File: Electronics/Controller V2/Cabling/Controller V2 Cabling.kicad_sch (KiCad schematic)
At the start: 12 parts, among them J1 Conn_01x30, J10 Spare Valve, J11 Battery, J2 GPIO, J3 Tractor CAN, J4 Scraper CAN, J5 Spare CAN, J6 Front Height, J7 Rear Height, J8 Front Apron/Dump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

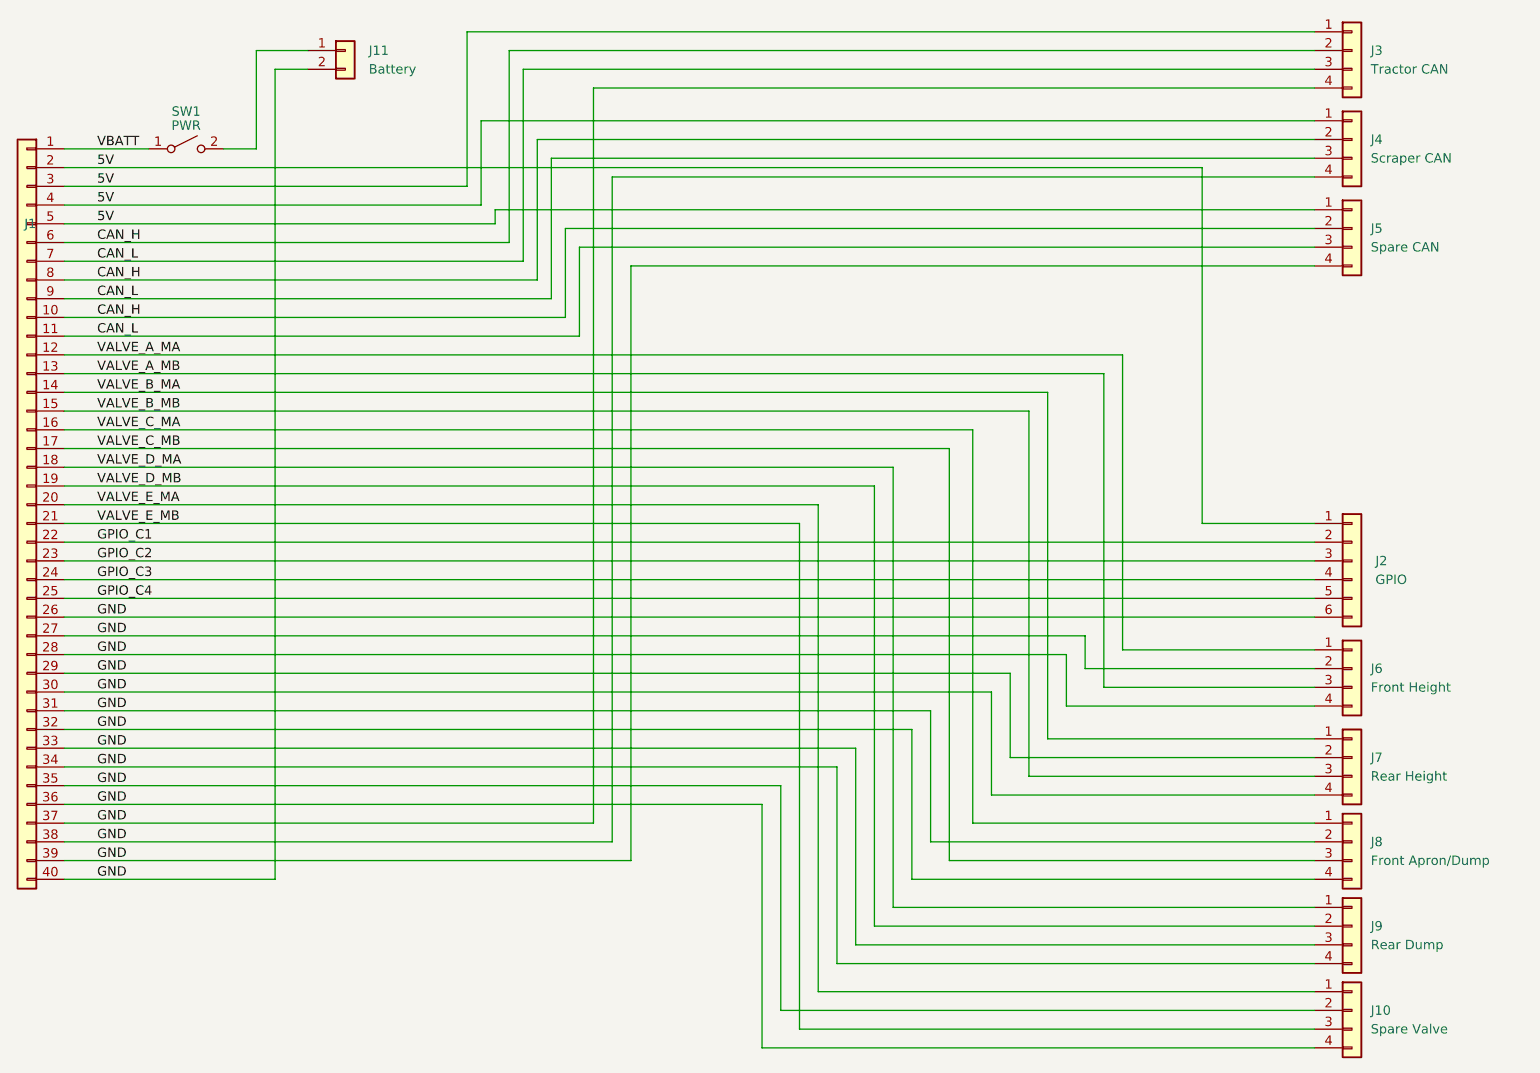
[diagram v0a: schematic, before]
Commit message: Reordered main connector.
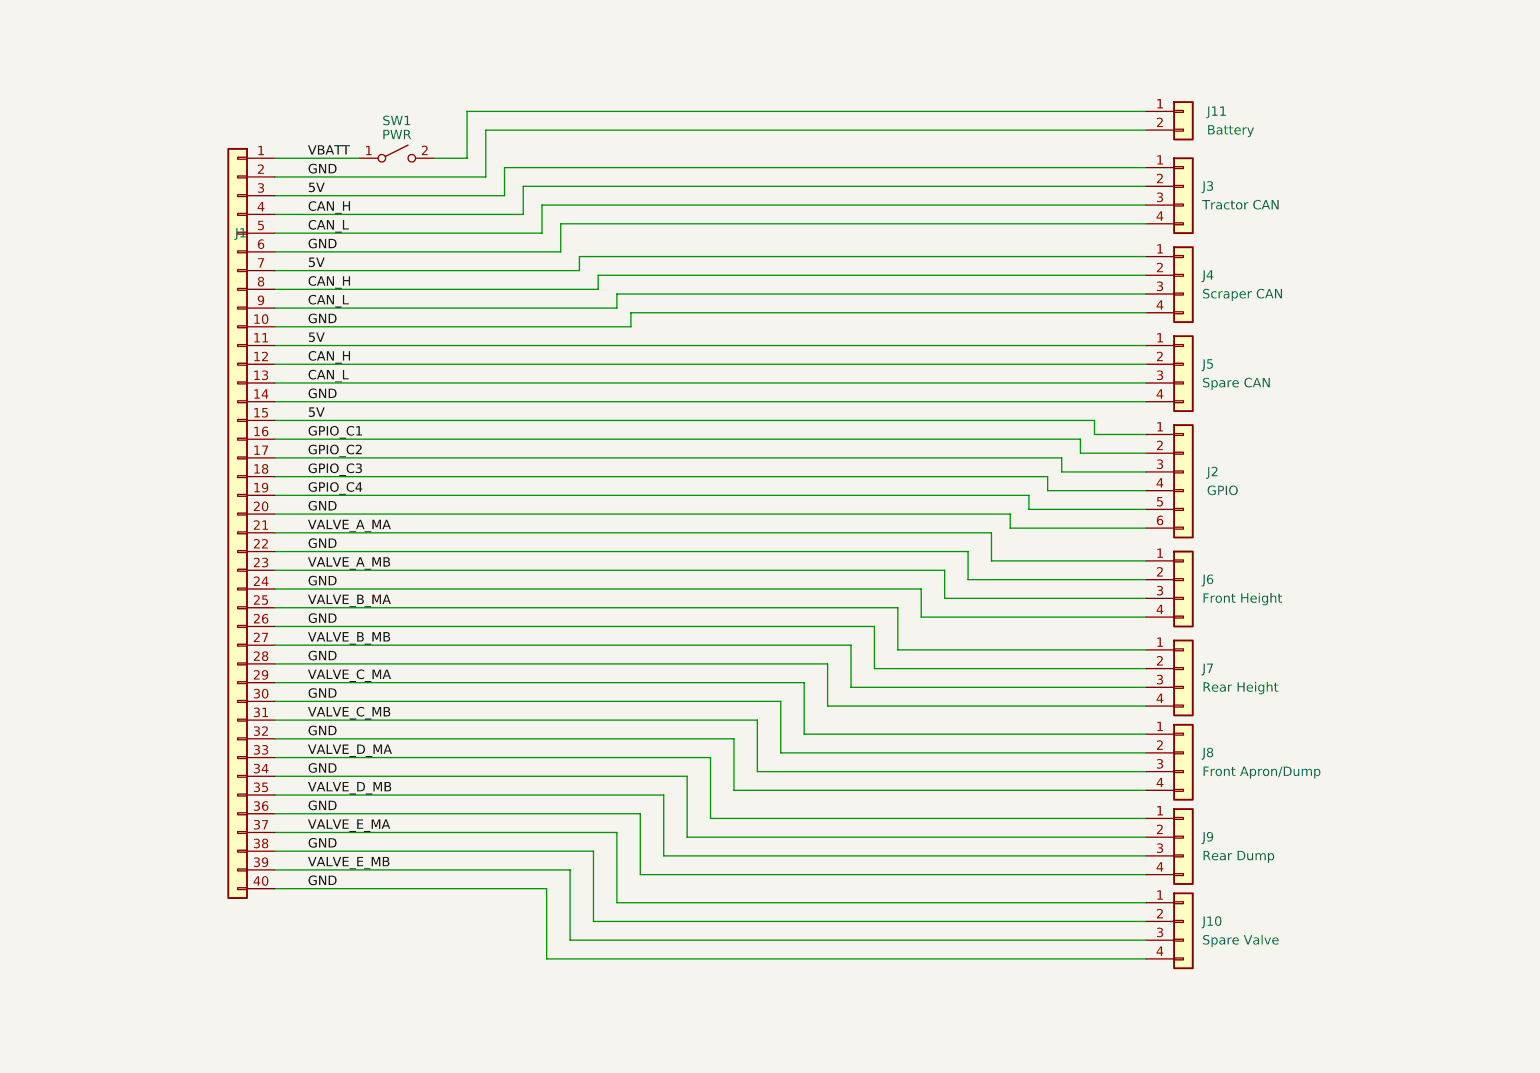
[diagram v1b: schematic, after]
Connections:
- net 5V: now also J1.11 (Pin_11), J1.15 (Pin_15), J1.7 (Pin_7); no longer J1.2 (Pin_2), J1.4 (Pin_4), J1.5 (Pin_5)
- net CAN_H: now also J1.12 (Pin_12), J1.4 (Pin_4); no longer J1.10 (Pin_10), J1.6 (Pin_6)
- net CAN_L: now also J1.13 (Pin_13), J1.5 (Pin_5); no longer J1.11 (Pin_11), J1.7 (Pin_7)
- net GND: now also J1.10 (Pin_10), J1.14 (Pin_14), J1.2 (Pin_2), J1.20 (Pin_20), J1.22 (Pin_22), J1.24 (Pin_24), J1.6 (Pin_6), J9.2 (Pin_2); no longer J1.27 (Pin_27), J1.29 (Pin_29), J1.31 (Pin_31), J1.33 (Pin_33), J1.35 (Pin_35), J1.37 (Pin_37), J1.39 (Pin_39), J9.3 (Pin_3)
- net GPIO_C1: now also J1.16 (Pin_16); no longer J1.22 (Pin_22)
- net GPIO_C2: now also J1.17 (Pin_17); no longer J1.23 (Pin_23)
- net GPIO_C3: now also J1.18 (Pin_18); no longer J1.24 (Pin_24)
- net GPIO_C4: now also J1.19 (Pin_19); no longer J1.25 (Pin_25)
- net VALVE_A_MA: now also J1.21 (Pin_21); no longer J1.12 (Pin_12)
- net VALVE_A_MB: now also J1.23 (Pin_23); no longer J1.13 (Pin_13)
- net VALVE_B_MA: now also J1.25 (Pin_25); no longer J1.14 (Pin_14)
- net VALVE_B_MB: now also J1.27 (Pin_27); no longer J1.15 (Pin_15)
- net VALVE_C_MA: now also J1.29 (Pin_29); no longer J1.16 (Pin_16)
- net VALVE_C_MB: now also J1.31 (Pin_31); no longer J1.17 (Pin_17)
- net VALVE_D_MA: now also J1.33 (Pin_33); no longer J1.18 (Pin_18)
- net VALVE_D_MB: now also J1.35 (Pin_35), J9.3 (Pin_3); no longer J1.19 (Pin_19), J9.2 (Pin_2)
- net VALVE_E_MA: now also J1.37 (Pin_37); no longer J1.20 (Pin_20)
- net VALVE_E_MB: now also J1.39 (Pin_39); no longer J1.21 (Pin_21)
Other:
- moved on the sheet: J1, J10, J11, J2, J3, J4, J5, J6, J7, J8, J9, SW1

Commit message: Added AMP connectors. Working on PCB layout.
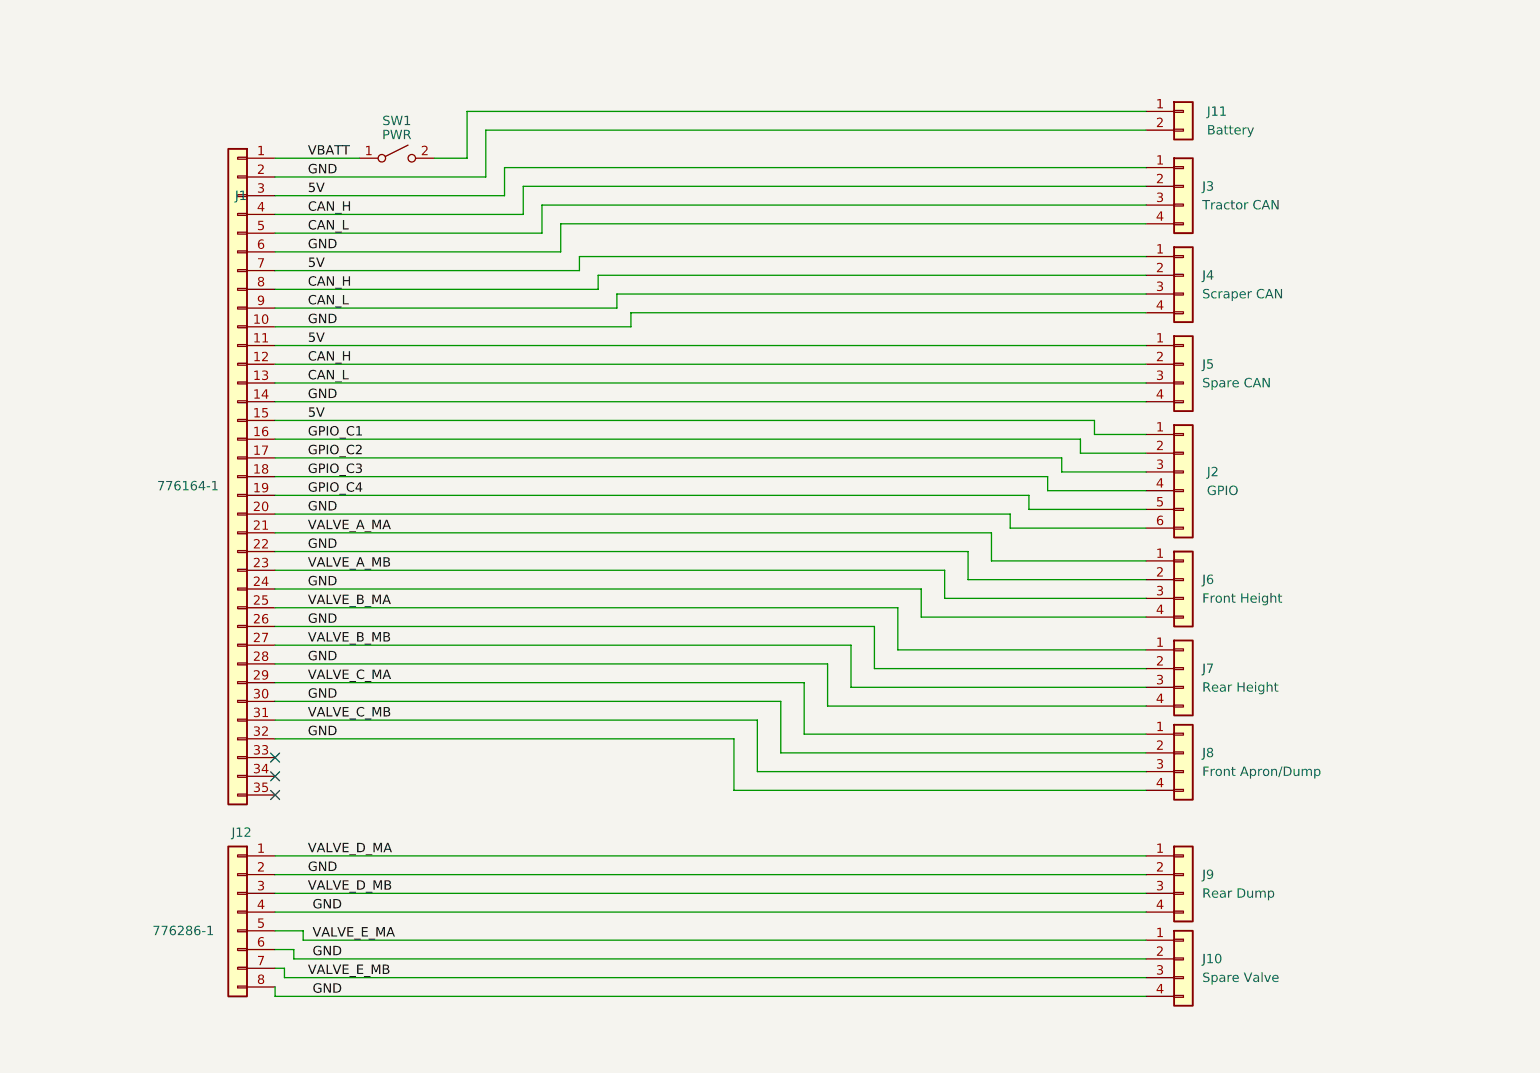
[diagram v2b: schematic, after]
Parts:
- added J12: 776286-1, symbol Connector_Generic:Conn_01x08
- J1: value Conn_01x30 -> 776164-1; symbol Connector_Generic:Conn_01x40 -> Connector_Generic:Conn_01x35
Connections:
- net GND: now also J12.2 (Pin_2), J12.4 (Pin_4), J12.6 (Pin_6), J12.8 (Pin_8); no longer J1.34 (Pin_34), J1.36 (Pin_36), J1.38 (Pin_38), J1.40 (Pin_40)
- net VALVE_D_MA: now also J12.1 (Pin_1); no longer J1.33 (Pin_33)
- net VALVE_D_MB: now also J12.3 (Pin_3); no longer J1.35 (Pin_35)
- net VALVE_E_MA: now also J12.5 (Pin_5); no longer J1.37 (Pin_37)
- net VALVE_E_MB: now also J12.7 (Pin_7); no longer J1.39 (Pin_39)
- no-connect marks 0 -> 3
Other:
- moved on the sheet: J10, J9

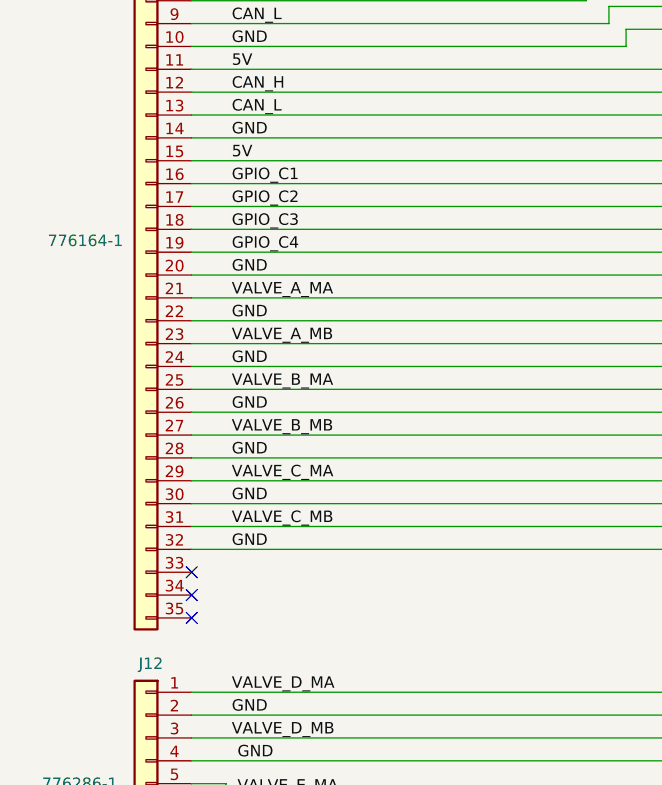
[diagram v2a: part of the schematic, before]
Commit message: Added missing ground connection. Working on PCB layout.
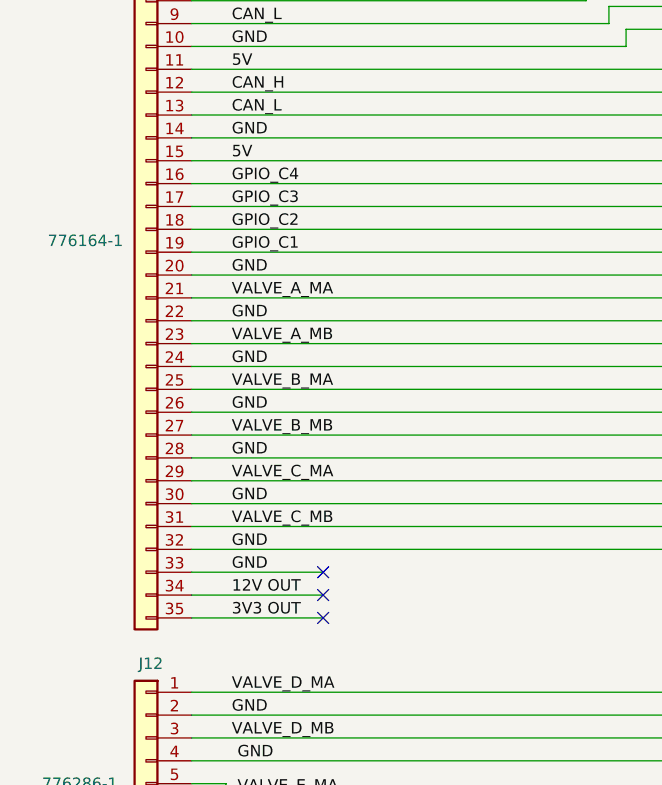
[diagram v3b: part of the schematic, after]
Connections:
- net GND: now also J1.33 (Pin_33)
- net GPIO_C1: now also J1.19 (Pin_19), J2.5 (Pin_5); no longer J1.16 (Pin_16), J2.2 (Pin_2)
- net GPIO_C2: now also J1.18 (Pin_18), J2.4 (Pin_4); no longer J1.17 (Pin_17), J2.3 (Pin_3)
- net GPIO_C3: now also J1.17 (Pin_17), J2.3 (Pin_3); no longer J1.18 (Pin_18), J2.4 (Pin_4)
- net GPIO_C4: now also J1.16 (Pin_16), J2.2 (Pin_2); no longer J1.19 (Pin_19), J2.5 (Pin_5)
- net 12V OUT: now reaches J1.34 (Pin_34)
- net 3V3 OUT: now reaches J1.35 (Pin_35)
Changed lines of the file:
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@@
     (comment 1 "NO WARRANTY, SUPPLIED AS-IS")
   )
-  (no_connect (at 83.82 121.92))
-  (no_connect (at 83.82 127))
-  (no_connect (at 83.82 124.46))
+  (no_connect (at 98.425 124.46))
+  (no_connect (at 98.425 121.92))
+  (no_connect (at 98.425 127))
   (wire (pts (xy 201.93 123.825) (xy 149.225 123.825))
     (stroke (width 0) (type default))
@@
     (stroke (width 0) (type default))
   )
+  (wire (pts (xy 83.82 121.92) (xy 98.425 121.92))
+    (stroke (width 0) (type default))
+  )
   (wire (pts (xy 201.93 41.91) (xy 114.935 41.91))
     (stroke (width 0) (type default))
@@
     (stroke (width 0) (type default))
   )
+  (wire (pts (xy 83.82 127) (xy 98.425 127))
+    (stroke (width 0) (type default))
+  )
   (wire (pts (xy 201.93 56.515) (xy 127.635 56.515))
     (stroke (width 0) (type default))
@@
     (stroke (width 0) (type default))
   )
+  (wire (pts (xy 83.82 124.46) (xy 98.425 124.46))
+    (stroke (width 0) (type default))
+  )
   (wire (pts (xy 201.93 59.055) (xy 130.175 59.055))
     (stroke (width 0) (type default))
@@
     (effects (font (size 1.27 1.27)) (justify left bottom))
   )
+  (label "GND" (at 88.265 121.92 0) (fields_autoplaced)
+    (effects (font (size 1.27 1.27)) (justify left bottom))
+  )
+  (label "12V OUT" (at 88.265 124.46 0) (fields_autoplaced)
+    (effects (font (size 1.27 1.27)) (justify left bottom))
+  )
   (label "VALVE_D_MA" (at 88.265 135.255 0) (fields_autoplaced)
     (effects (font (size 1.27 1.27)) (justify left bottom))
@@
     (effects (font (size 1.27 1.27)) (justify left bottom))
   )
-  (label "GPIO_C3" (at 88.265 83.82 0) (fields_autoplaced)
+  (label "GPIO_C3" (at 88.265 81.28 0) (fields_autoplaced)
     (effects (font (size 1.27 1.27)) (justify left bottom))
   )
@@
     (effects (font (size 1.27 1.27)) (justify left bottom))
   )
-  (label "GPIO_C4" (at 88.265 86.36 0) (fields_autoplaced)
+  (label "GPIO_C4" (at 88.265 78.74 0) (fields_autoplaced)
     (effects (font (size 1.27 1.27)) (justify left bottom))
   )
@@
     (effects (font (size 1.27 1.27)) (justify left bottom))
   )
-  (label "GPIO_C2" (at 88.265 81.28 0) (fields_autoplaced)
+  (label "3V3 OUT" (at 88.265 127 0) (fields_autoplaced)
+    (effects (font (size 1.27 1.27)) (justify left bottom))
+  )
+  (label "GPIO_C2" (at 88.265 83.82 0) (fields_autoplaced)
     (effects (font (size 1.27 1.27)) (justify left bottom))
   )
@@
     (effects (font (size 1.27 1.27)) (justify left bottom))
   )
-  (label "GPIO_C1" (at 88.265 78.74 0) (fields_autoplaced)
-    (effects (font (size 1.27 1.27)) (justify left bottom))
-  )
+  (label "GPIO_C1" (at 88.265 86.36 0) (fields_autoplaced)
+    (effects (font (size 1.27 1.27)) (justify left bottom))
+  )
